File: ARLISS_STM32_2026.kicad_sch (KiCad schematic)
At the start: 0 parts

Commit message: 21/05
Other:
- added sheet CORE_STM32F405 (EsquemáticoSTM32F405.kicad_sch)
- added sheet DPS310 Sheet (Barómetro DPS310.kicad_sch)
- added sheet DriverDRV8874 (DriverDRV8874.kicad_sch)
- added sheet IMU BNO085 (IMU.kicad_sch)
- added sheet VEML 7700 Sheet (SensorLuz_VEML7700.kicad_sch)

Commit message: 22/05
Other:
- added sheet Alimentacion (untitled.kicad_sch)
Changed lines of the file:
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@@
 	)
 	(sheet
-		(at 110.49 74.93)
+		(at 170.18 69.85)
+		(size 40.64 25.4)
+		(exclude_from_sim no)
+		(in_bom yes)
+		(on_board yes)
+		(dnp no)
+		(fields_autoplaced yes)
+		(stroke
+			(width 0.1524)
+			(type solid)
+		)
+		(fill
+			(color 0 0 0 0)
+		)
+		(property "Sheetname" "Alimentacion"
+			(at 170.18 69.1384 0)
+			(show_name no)
+			(do_not_autoplace no)
+			(effects
+				(font
+					(size 1.27 1.27)
+				)
+				(justify left bottom)
+			)
+		)
+		(property "Sheetfile" "untitled.kicad_sch"
+			(at 170.18 95.8346 0)
+			(show_name no)
+			(do_not_autoplace no)
+			(effects
+				(font
+					(size 1.27 1.27)
+				)
+				(justify left top)
+			)
+		)
+		(instances
+			(project "ARLISS_STM32_2026"
+				(path "/9719ea46-14c4-4409-9c57-49dd5454c03f"
+					(page "7")
+				)
+			)
+		)
+	)
+	(sheet
+		(at 114.3 71.12)
 		(size 33.02 24.13)
 		(exclude_from_sim no)
@@
 		)
 		(property "Sheetname" "VEML 7700 Sheet"
-			(at 110.49 74.2184 0)
+			(at 114.3 70.4084 0)
 			(show_name no)
 			(do_not_autoplace no)
@@
 		)
 		(property "Sheetfile" "SensorLuz_VEML7700.kicad_sch"
-			(at 110.49 99.6446 0)
+			(at 114.3 95.8346 0)
 			(show_name no)
 			(do_not_autoplace no)

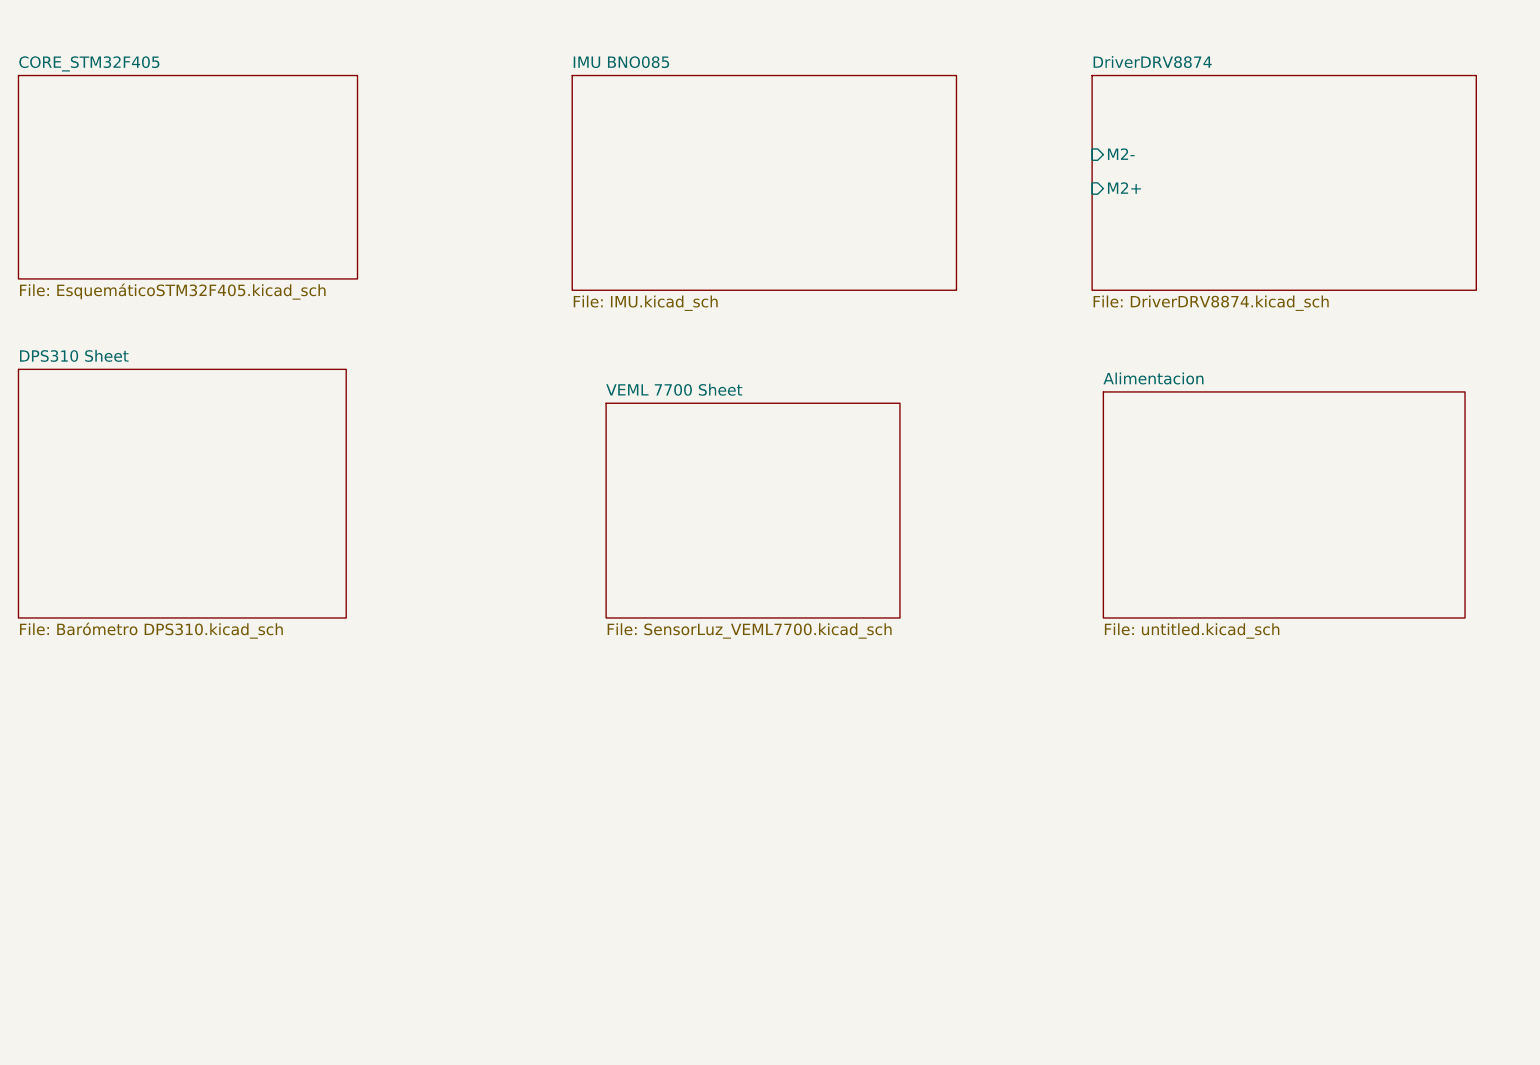
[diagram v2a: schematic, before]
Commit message: Protocolos I2C/SPI
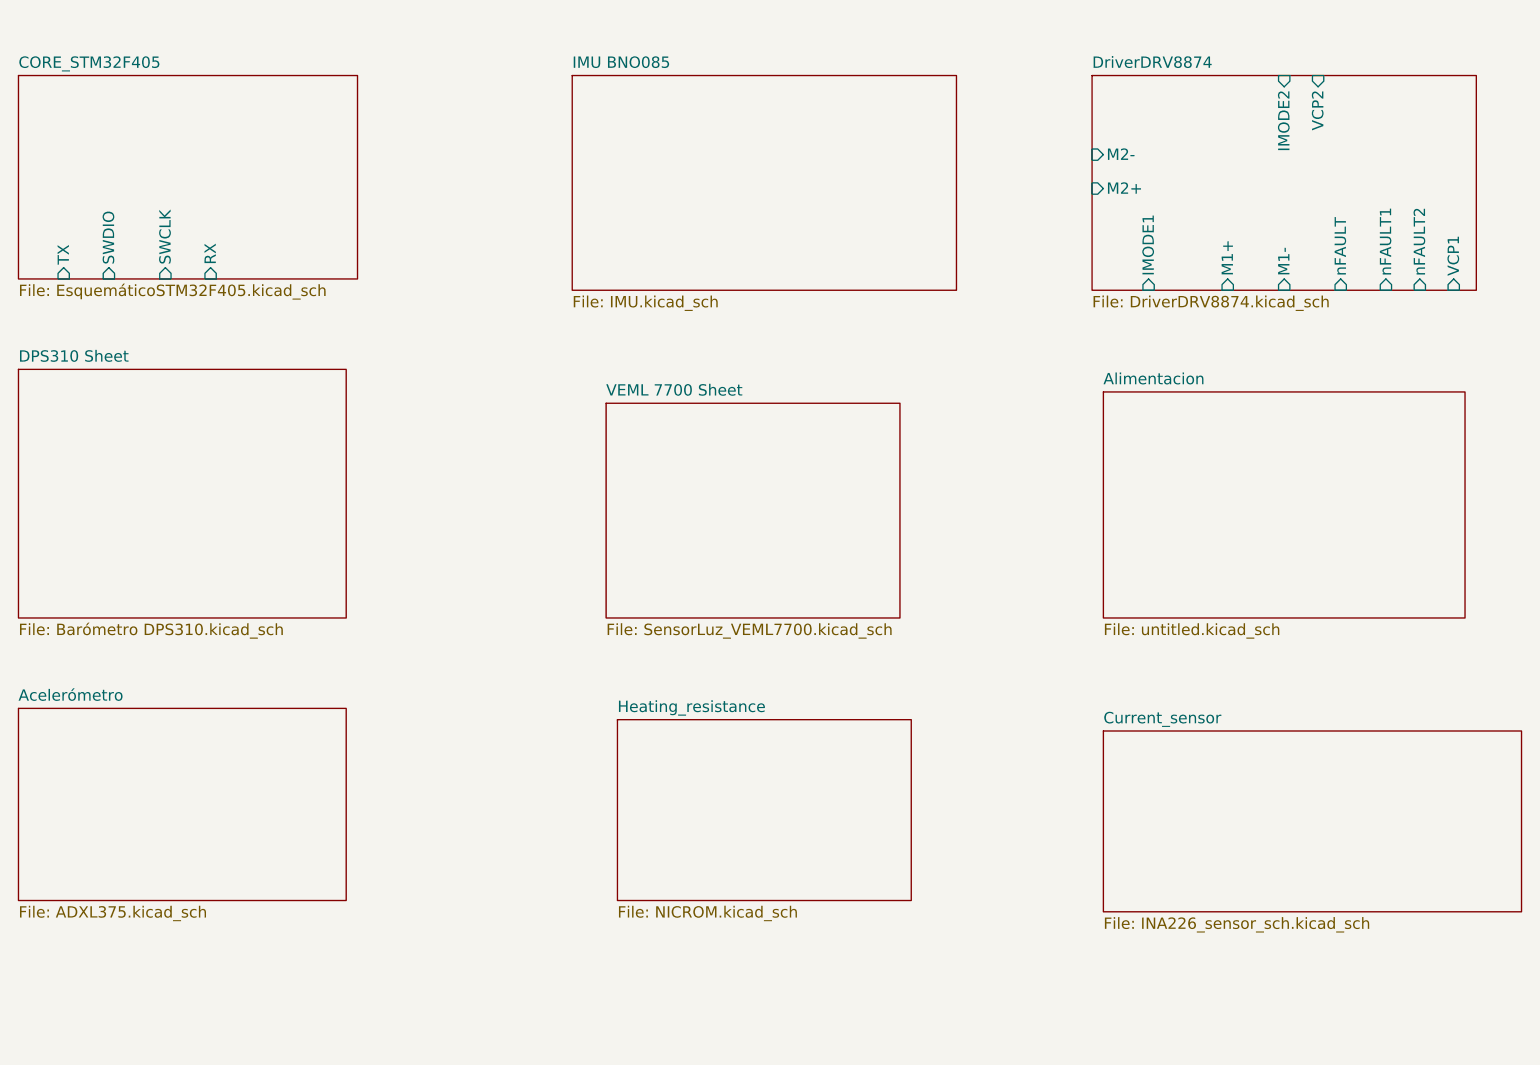
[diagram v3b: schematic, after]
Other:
- added sheet Acelerómetro (ADXL375.kicad_sch)
- added sheet Current_sensor (INA226_sensor_sch.kicad_sch)
- added sheet Heating_resistance (NICROM.kicad_sch)
- sheet CORE_STM32F405 ports: added RX, SWCLK, SWDIO, TX; removed none
- sheet DriverDRV8874 ports: added IMODE1, IMODE2, M1+, M1-, VCP1, VCP2, nFAULT, nFAULT1, nFAULT2; removed none

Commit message: feat: [solución de rules checker]
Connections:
- no-connect marks 0 -> 16
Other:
- sheet VEML 7700 Sheet ports: added VDD_LUZ; removed none
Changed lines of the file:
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@@
 	(generator_version "10.0")
 	(paper "A4")
+	(no_connect
+		(at 205.74 58.42)
+	)
+	(no_connect
+		(at 184.15 58.42)
+	)
+	(no_connect
+		(at 58.42 57.15)
+	)
+	(no_connect
+		(at 53.34 57.15)
+	)
+	(no_connect
+		(at 175.26 58.42)
+	)
+	(no_connect
+		(at 64.77 57.15)
+	)
+	(no_connect
+		(at 196.85 58.42)
+	)
+	(no_connect
+		(at 69.85 57.15)
+	)
+	(no_connect
+		(at 190.5 58.42)
+	)
+	(no_connect
+		(at 201.93 58.42)
+	)
+	(no_connect
+		(at 194.31 34.29)
+	)
+	(no_connect
+		(at 168.91 46.99)
+	)
+	(no_connect
+		(at 168.91 43.18)
+	)
+	(no_connect
+		(at 114.3 81.28)
+	)
+	(no_connect
+		(at 190.5 34.29)
+	)
+	(no_connect
+		(at 209.55 58.42)
+	)
 	(sheet
 		(at 110.49 34.29)
@@
 			)
 		)
+		(pin "VDD_LUZ" input
+			(at 114.3 81.28 180)
+			(effects
+				(font
+					(size 1.27 1.27)
+				)
+				(justify left)
+			)
+		)

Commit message: Actualización de nets
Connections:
- no-connect marks 16 -> 12
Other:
- sheet DriverDRV8874 renamed Motor control
- sheet CORE_STM32F405 ports: added none; removed RX, SWCLK, SWDIO, TX
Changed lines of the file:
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@@
-	)
-	(no_connect
-		(at 58.42 57.15)
-	)
-	(no_connect
-		(at 53.34 57.15)
 	)
 	(no_connect
@@
 	)
 	(no_connect
-		(at 64.77 57.15)
-	)
-	(no_connect
 		(at 196.85 58.42)
 	)
 	(no_connect
-		(at 69.85 57.15)
-	)
-	(no_connect
 		(at 190.5 58.42)
 	)
@@
 	)
 	(sheet
-		(at 110.49 34.29)
-		(size 43.18 24.13)
+		(at 125.73 40.64)
+		(size 20.32 13.97)
 		(exclude_from_sim no)
 		(in_bom yes)
@@
 		)
 		(property "Sheetname" "IMU BNO085"
-			(at 110.49 33.5784 0)
+			(at 125.73 39.9284 0)
 			(show_name no)
 			(do_not_autoplace no)
@@
 		)
 		(property "Sheetfile" "IMU.kicad_sch"
-			(at 110.49 59.0046 0)
+			(at 125.73 55.1946 0)
 			(show_name no)
 			(do_not_autoplace no)
@@
 			(color 0 0 0 0)
 		)
-		(property "Sheetname" "DriverDRV8874"
+		(property "Sheetname" "Motor control"
 			(at 168.91 33.5784 0)
 			(show_name no)
@@
 			)
 		)
-		(pin "RX" input
-			(at 69.85 57.15 270)
-			(effects
-				(font
-					(size 1.27 1.27)
-				)
-				(justify left)
-			)
-		)
-		(pin "SWCLK" input
-			(at 64.77 57.15 270)
-			(effects
-				(font
-					(size 1.27 1.27)
-				)
-				(justify left)
-			)
-		)
-		(pin "SWDIO" input
-			(at 58.42 57.15 270)
-			(effects
-				(font
-					(size 1.27 1.27)
-				)
-				(justify left)
-			)
-		)
-		(pin "TX" input
-			(at 53.34 57.15 270)
-			(effects
-				(font
-					(size 1.27 1.27)
-				)
-				(justify left)
-			)
-		)

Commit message: Cantidad de errores en la PCB: 29
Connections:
- no-connect marks 12 -> 8
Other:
- sheet Motor control ports: added none; removed M1+, M1-, M2+, M2-
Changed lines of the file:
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@@
-	)
-	(no_connect
-		(at 184.15 58.42)
 	)
 	(no_connect
@@
 	)
 	(no_connect
-		(at 190.5 58.42)
-	)
-	(no_connect
 		(at 201.93 58.42)
 	)
 	(no_connect
 		(at 194.31 34.29)
-	)
-	(no_connect
-		(at 168.91 46.99)
-	)
-	(no_connect
-		(at 168.91 43.18)
 	)
 	(no_connect
@@
 			)
 		)
-		(pin "M2-" input
-			(at 168.91 43.18 180)
-			(effects
-				(font
-					(size 1.27 1.27)
-				)
-				(justify left)
-			)
-		)
-		(pin "M2+" input
-			(at 168.91 46.99 180)
-			(effects
-				(font
-					(size 1.27 1.27)
-				)
-				(justify left)
-			)
-		)
 		(pin "IMODE2" input
 			(at 190.5 34.29 90)
@@
 			(effects
 				(font
-					(size 1.27 1.27)
-				)
-				(justify left)
-			)
-		)
-		(pin "M1+" input
-			(at 184.15 58.42 270)
-			(effects
-				(font
-					(size 1.27 1.27)
-				)
-				(justify left)
-			)
-		)
-		(pin "M1-" input
-			(at 190.5 58.42 270)
-			(effects
-				(font

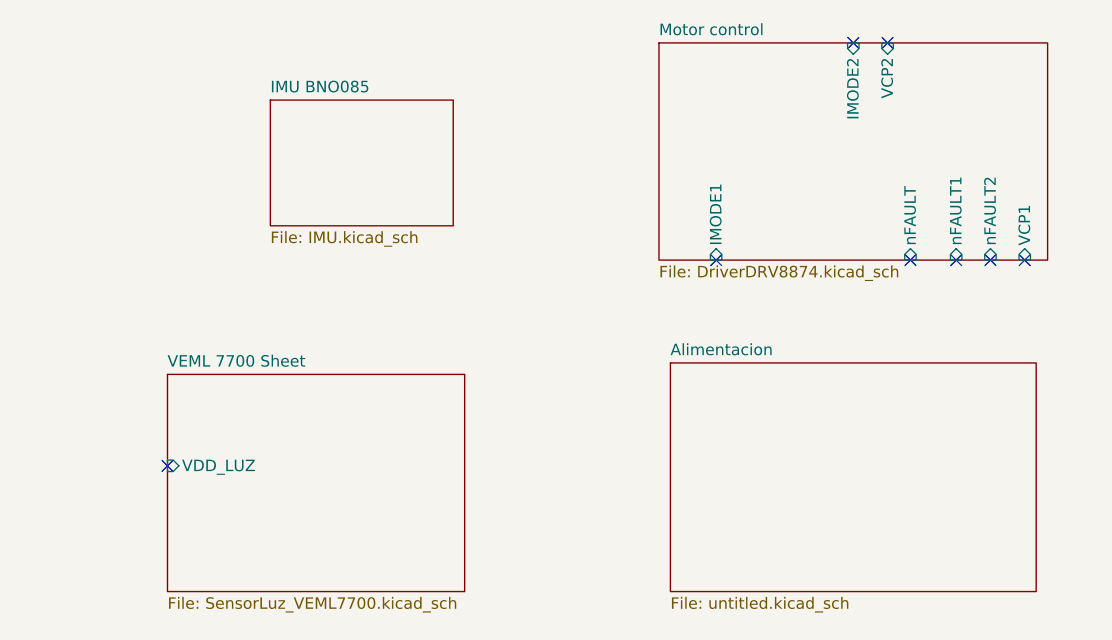
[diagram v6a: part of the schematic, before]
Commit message: Esquemático Versión mejorada
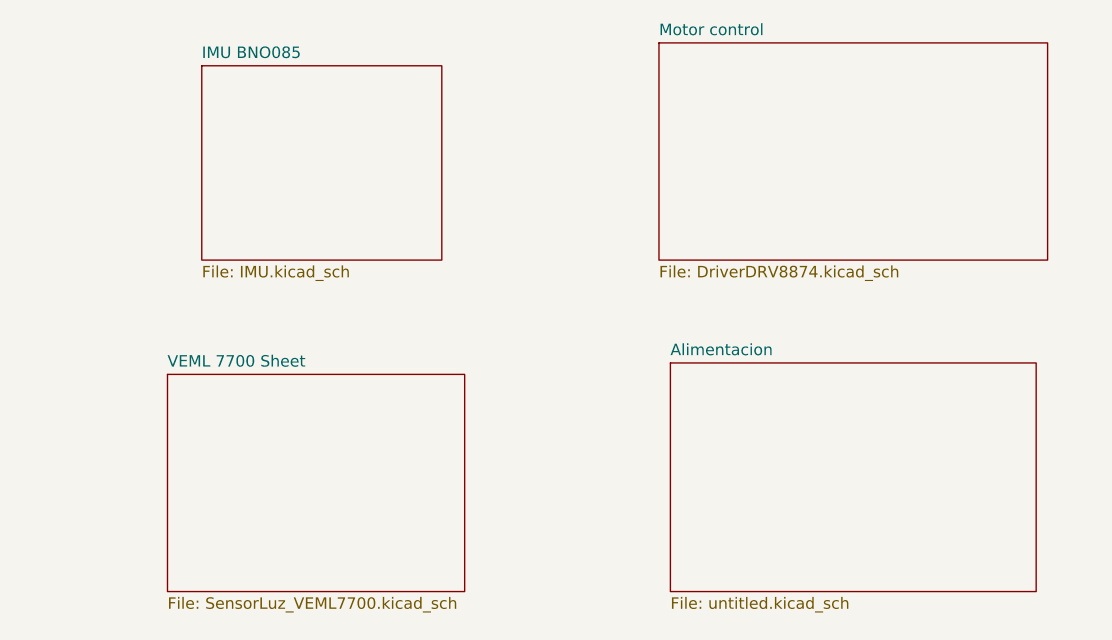
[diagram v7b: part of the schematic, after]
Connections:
- no-connect marks 8 -> 0
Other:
- sheet Motor control ports: added none; removed IMODE1, IMODE2, VCP1, VCP2, nFAULT, nFAULT1, nFAULT2
- sheet VEML 7700 Sheet ports: added none; removed VDD_LUZ
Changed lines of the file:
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@@
 	(generator_version "10.0")
 	(paper "A4")
-	(no_connect
-		(at 205.74 58.42)
-	)
-	(no_connect
-		(at 175.26 58.42)
-	)
-	(no_connect
-		(at 196.85 58.42)
-	)
-	(no_connect
-		(at 201.93 58.42)
-	)
-	(no_connect
-		(at 194.31 34.29)
-	)
-	(no_connect
-		(at 114.3 81.28)
-	)
-	(no_connect
-		(at 190.5 34.29)
-	)
-	(no_connect
-		(at 209.55 58.42)
-	)
-	(sheet
-		(at 125.73 40.64)
-		(size 20.32 13.97)
+	(sheet
+		(at 118.11 36.83)
+		(size 26.67 21.59)
 		(exclude_from_sim no)
 		(in_bom yes)
@@
 		)
 		(property "Sheetname" "IMU BNO085"
-			(at 125.73 39.9284 0)
+			(at 118.11 36.1184 0)
 			(show_name no)
 			(do_not_autoplace no)
@@
 		)
 		(property "Sheetfile" "IMU.kicad_sch"
-			(at 125.73 55.1946 0)
+			(at 118.11 59.0046 0)
 			(show_name no)
 			(do_not_autoplace no)
@@
 				)
 				(justify left top)
-			)
-		)
-		(pin "IMODE2" input
-			(at 190.5 34.29 90)
-			(effects
-				(font
-					(size 1.27 1.27)
-				)
-				(justify right)
-			)
-		)
-		(pin "VCP2" input
-			(at 194.31 34.29 90)
-			(effects
-				(font
-					(size 1.27 1.27)
-				)
-				(justify right)
-			)
-		)
-		(pin "IMODE1" input
-			(at 175.26 58.42 270)
-			(effects
-				(font
-					(size 1.27 1.27)
-				)
-				(justify left)
-			)
-		)
-		(pin "nFAULT" input
-			(at 196.85 58.42 270)
-			(effects
-				(font
-					(size 1.27 1.27)
-				)
-				(justify left)
-			)
-		)
-		(pin "nFAULT1" input
-			(at 201.93 58.42 270)
-			(effects
-				(font
-					(size 1.27 1.27)
-				)
-				(justify left)
-			)
-		)
-		(pin "nFAULT2" input
-			(at 205.74 58.42 270)
-			(effects
-				(font
-					(size 1.27 1.27)
-				)
-				(justify left)
-			)
-		)
-		(pin "VCP1" input
-			(at 209.55 58.42 270)
-			(effects
-				(font
-					(size 1.27 1.27)
-				)
-				(justify left)
 			)
 		)
@@
 			)
 		)
-		(pin "VDD_LUZ" input
-			(at 114.3 81.28 180)
-			(effects
-				(font
-					(size 1.27 1.27)
-				)
-				(justify left)
-			)
-		)

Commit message: PCB ordenada V1
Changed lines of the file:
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@@
 	(generator_version "10.0")
 	(paper "A4")
-	(sheet
-		(at 118.11 36.83)
-		(size 26.67 21.59)
+	(text_box "SPI_1 INTERFACE"
+		(exclude_from_sim no)
+		(at 110.49 27.8017 0)
+		(size 50.8 34.4283)
+		(margins 0.9525 0.9525 0.9525 0.9525)
+		(stroke
+			(width 0)
+			(type solid)
+		)
+		(fill
+			(type none)
+		)
+		(effects
+			(font
+				(size 1.27 1.27)
+			)
+			(justify left top)
+		)
+	)
+	(text_box "SPI_2 INTERFACE"
+		(exclude_from_sim no)
+		(at 167.64 27.94 0)
+		(size 44.45 34.2899)
+		(margins 0.9525 0.9525 0.9525 0.9525)
+		(stroke
+			(width 0)
+			(type solid)
+		)
+		(fill
+			(type none)
+		)
+		(effects
+			(font
+				(size 1.27 1.27)
+			)
+			(justify left top)
+		)
+	)
+	(text_box "I2C_1"
+		(exclude_from_sim no)
+		(at 53.34 71.12 0)
+		(size 48.26 72.39)
+		(margins 0.9525 0.9525 0.9525 0.9525)
+		(stroke
+			(width 0)
+			(type solid)
+		)
+		(fill
+			(type none)
+		)
+		(effects
+			(font
+				(size 1.27 1.27)
+			)
+			(justify left top)
+		)
+	)
+	(sheet
+		(at 114.3 36.83)
+		(size 40.64 21.59)
 		(exclude_from_sim no)
 		(in_bom yes)
@@
 		)
 		(property "Sheetname" "IMU BNO085"
-			(at 118.11 36.1184 0)
+			(at 114.3 36.1184 0)
 			(show_name no)
 			(do_not_autoplace no)
@@
 		)
 		(property "Sheetfile" "IMU.kicad_sch"
-			(at 118.11 59.0046 0)
+			(at 114.3 59.0046 0)
 			(show_name no)
 			(do_not_autoplace no)
@@
 	)
 	(sheet
-		(at 168.91 34.29)
-		(size 43.18 24.13)
+		(at 143.51 106.68)
+		(size 38.1 20.32)
 		(exclude_from_sim no)
 		(in_bom yes)
@@
 		)
 		(property "Sheetname" "Motor control"
-			(at 168.91 33.5784 0)
+			(at 143.51 105.9684 0)
 			(show_name no)
 			(do_not_autoplace no)
@@
 		)
 		(property "Sheetfile" "DriverDRV8874.kicad_sch"
-			(at 168.91 59.0046 0)
+			(at 143.51 127.5846 0)
 			(show_name no)
 			(do_not_autoplace no)
@@
 	)
 	(sheet
-		(at 115.57 106.68)
-		(size 33.02 20.32)
+		(at 167.64 76.2)
+		(size 41.91 20.32)
 		(exclude_from_sim no)
 		(in_bom yes)
@@
 		)
 		(property "Sheetname" "Heating_resistance"
-			(at 115.57 105.9684 0)
+			(at 167.64 75.4884 0)
 			(show_name no)
 			(do_not_autoplace no)
@@
 		)
 		(property "Sheetfile" "NICROM.kicad_sch"
-			(at 115.57 127.5846 0)
+			(at 167.64 97.1046 0)
 			(show_name no)
 			(do_not_autoplace no)
@@
 	)
 	(sheet
-		(at 48.26 105.41)
+		(at 170.18 36.83)
 		(size 36.83 21.59)
 		(exclude_from_sim no)
@@
 		)
 		(property "Sheetname" "Acelerómetro"
-			(at 48.26 104.6984 0)
+			(at 170.18 36.1184 0)
 			(show_name no)
 			(do_not_autoplace no)
@@
 		)
 		(property "Sheetfile" "ADXL375.kicad_sch"
-			(at 48.26 127.5846 0)
+			(at 170.18 59.0046 0)
 			(show_name no)
 			(do_not_autoplace no)
@@
 	)
 	(sheet
-		(at 170.18 69.85)
+		(at 116.84 73.66)
 		(size 40.64 25.4)
 		(exclude_from_sim no)
@@
 		)
 		(property "Sheetname" "Alimentacion"
-			(at 170.18 69.1384 0)
+			(at 116.84 72.9484 0)
 			(show_name no)
 			(do_not_autoplace no)
@@
 		)
 		(property "Sheetfile" "untitled.kicad_sch"
-			(at 170.18 95.8346 0)
+			(at 116.84 99.6446 0)
 			(show_name no)
 			(do_not_autoplace no)
@@
 	)
 	(sheet
-		(at 114.3 71.12)
-		(size 33.02 24.13)
+		(at 77.47 115.57)
+		(size 16.51 12.7)
 		(exclude_from_sim no)
 		(in_bom yes)
@@
 		)
 		(property "Sheetname" "VEML 7700 Sheet"
-			(at 114.3 70.4084 0)
+			(at 77.47 114.8584 0)
 			(show_name no)
 			(do_not_autoplace no)
@@
 		)
 		(property "Sheetfile" "SensorLuz_VEML7700.kicad_sch"
-			(at 114.3 95.8346 0)
+			(at 77.47 128.8546 0)
+			(hide yes)
 			(show_name no)
 			(do_not_autoplace no)
@@
 	)
 	(sheet
-		(at 48.26 67.31)
+		(at 57.15 77.47)
 		(size 36.83 27.94)
 		(exclude_from_sim no)
@@
 		)
 		(property "Sheetname" "DPS310 Sheet"
-			(at 48.26 66.5984 0)
+			(at 57.15 76.7584 0)
 			(show_name no)
 			(do_not_autoplace no)
@@
 		)
 		(property "Sheetfile" "Barómetro DPS310.kicad_sch"
-			(at 48.26 95.8346 0)
+			(at 57.15 105.9946 0)
 			(show_name no)
 			(do_not_autoplace no)
@@
 	)
 	(sheet
-		(at 170.18 107.95)
-		(size 46.99 20.32)
+		(at 57.15 115.57)
+		(size 13.97 12.7)
 		(exclude_from_sim no)
 		(in_bom yes)
@@
 		)
 		(property "Sheetname" "Current_sensor"
-			(at 170.18 107.2384 0)
+			(at 57.15 114.8584 0)
 			(show_name no)
 			(do_not_autoplace no)
@@
 		)
 		(property "Sheetfile" "INA226_sensor_sch.kicad_sch"
-			(at 170.18 128.8546 0)
-			(show_name no)
-			(do_not_autoplace no)
+			(at 57.15 128.8546 0)
+			(hide yes)
+			(show_name no)
+			(do_not_autoplace no)
